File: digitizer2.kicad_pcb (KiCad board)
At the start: 2 copper layers, 3 parts, among them U1 XC7A35T, U3 MT41K128M16, U4 ADS5403

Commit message: Initial routing
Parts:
- moved U4 24.7 mm to (160.0, 120.0), turned to 270 degrees
- moved U1 22.5 mm to (160.0, 95.0), turned to 135 degrees
- moved U3 18.7 mm to (140.0, 95.0), turned to 180 degrees
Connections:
- net Net-(U1-PadL7) renamed /JTAG_TCK
- net Net-(U1-PadM7) renamed /JTAG_TMS
- net Net-(U1-PadN7) renamed /JTAG_TDI
- net Net-(U1-PadN8) renamed /JTAG_TDO
- net Net-(U3-PadA2) renamed /DRAM_DQ13
- net Net-(U3-PadA3) renamed /DRAM_DQ15
- net Net-(U3-PadA7) renamed /DRAM_DQ12
- net Net-(U3-PadB7) renamed /DRAM_DQS1_N
- net Net-(U3-PadB8) renamed /DRAM_DQ14
- net Net-(U3-PadC2) renamed /DRAM_DQ11
- net Net-(U3-PadC3) renamed /DRAM_DQ9
- net Net-(U3-PadC7) renamed /DRAM_DQS1_P
- net Net-(U3-PadC8) renamed /DRAM_DQ10
- net Net-(U3-PadD3) renamed /DRAM_DM1
- net Net-(U3-PadD7) renamed /DRAM_DQ8
- net Net-(U3-PadE3) renamed /DRAM_DQ0
- net Net-(U3-PadE7) renamed /DRAM_DM0
- net Net-(U3-PadF2) renamed /DRAM_DQ2
- net Net-(U3-PadF3) renamed /DRAM_DQS0_P
- net Net-(U3-PadF7) renamed /DRAM_DQ1
- net Net-(U3-PadF8) renamed /DRAM_DQ3
- net Net-(U3-PadG2) renamed /DRAM_DQ6
- net Net-(U3-PadG3) renamed /DRAM_DQS0_N
- net Net-(U3-PadH3) renamed /DRAM_DQ4
- net Net-(U3-PadH7) renamed /DRAM_DQ7
- net Net-(U3-PadH8) renamed /DRAM_DQ5
- net Net-(U3-PadJ3) renamed /DRAM_RAS
- net Net-(U3-PadJ7) renamed /DRAM_CK_P
- net Net-(U3-PadK1) renamed /DRAM_ODT
- net Net-(U3-PadK3) renamed /DRAM_CAS
- net Net-(U3-PadK7) renamed /DRAM_CK_N
- net Net-(U3-PadK9) renamed /DRAM_CKE
- net Net-(U3-PadL2) renamed /DRAM_CS
- net Net-(U3-PadL3) renamed /DRAM_WE
- net Net-(U3-PadL7) renamed /DRAM_A10
- net Net-(U3-PadL8) renamed /DRAM_ZQ
- net Net-(U3-PadM2) renamed /DRAM_BA0
- net Net-(U3-PadM3) renamed /DRAM_BA2
- net Net-(U3-PadN2) renamed /DRAM_A3
- net Net-(U3-PadN3) renamed /DRAM_A0
- net Net-(U3-PadN7) renamed /DRAM_A12
- net Net-(U3-PadN8) renamed /DRAM_BA1
- net Net-(U3-PadP2) renamed /DRAM_A5
- net Net-(U3-PadP3) renamed /DRAM_A2
- net Net-(U3-PadP7) renamed /DRAM_A1
- net Net-(U3-PadP8) renamed /DRAM_A4
- net Net-(U3-PadR2) renamed /DRAM_A7
- net Net-(U3-PadR3) renamed /DRAM_A9
- net Net-(U3-PadR7) renamed /DRAM_A11
- net Net-(U3-PadR8) renamed /DRAM_A6
- net Net-(U3-PadT2) renamed /DRAM_RESET
- net Net-(U3-PadT3) renamed /DRAM_A13
- net Net-(U3-PadT8) renamed /DRAM_A8
- net Net-(U4-PadA10) renamed /ADC_SDO
- net Net-(U4-PadA11) renamed /ADC_SDIO
- net Net-(U4-PadA12) renamed /ADC_SCLK
- net Net-(U4-PadA13) renamed /ADC_SDENB
- net Net-(U4-PadH1) renamed /ADC_DACLK_N
- net Net-(U4-PadH2) renamed /ADC_DACLK_P
- net Net-(U4-PadH3) renamed /ADC_DA0_N
- net Net-(U4-PadH4) renamed /ADC_DA0_P
- net Net-(U4-PadJ1) renamed /ADC_DA1_N
- net Net-(U4-PadJ2) renamed /ADC_DA1_P
- net Net-(U4-PadJ3) renamed /ADC_DA2_N
- net Net-(U4-PadJ4) renamed /ADC_DA2_P
- net Net-(U4-PadK1) renamed /ADC_DA3_N
- net Net-(U4-PadK2) renamed /ADC_DA3_P
- net Net-(U4-PadK3) renamed /ADC_DA4_N
- net Net-(U4-PadK4) renamed /ADC_DA4_P
- net Net-(U4-PadL1) renamed /ADC_DA5_N
- net Net-(U4-PadL2) renamed /ADC_DA5_P
- net Net-(U4-PadL3) renamed /ADC_DA6_N
- net Net-(U4-PadL4) renamed /ADC_DA6_P
- net Net-(U4-PadL5) renamed /ADC_OVRA_N
- net Net-(U4-PadM1) renamed /ADC_DA7_N
- net Net-(U4-PadM2) renamed /ADC_DA7_P
- net Net-(U4-PadM3) renamed /ADC_DA8_N
- net Net-(U4-PadM4) renamed /ADC_DA8_P
- net Net-(U4-PadM5) renamed /ADC_OVRA_P
- net Net-(U4-PadN1) renamed /ADC_DA9_N
- net Net-(U4-PadN2) renamed /ADC_DA10_N
- net Net-(U4-PadN3) renamed /ADC_DA11_N
- net Net-(U4-PadP1) renamed /ADC_DA9_P
- net Net-(U4-PadP2) renamed /ADC_DA10_P
- net Net-(U4-PadP3) renamed /ADC_DA11_P
- U3 pad A8: Net-(U3-PadA8) -> Net-(U3-PadA1)
- U3 pad B3: Net-(U3-PadB3) -> Net-(U3-PadA9)
- U3 pad B9: Net-(U3-PadB9) -> Net-(U3-PadB1)
- U3 pad C1: Net-(U3-PadC1) -> Net-(U3-PadA1)
- U3 pad C9: Net-(U3-PadC9) -> Net-(U3-PadA1)
- U3 pad D1: Net-(U3-PadD1) -> Net-(U3-PadB1)
- U3 pad D2: Net-(U3-PadD2) -> Net-(U3-PadA1)
- U3 pad D8: Net-(U3-PadD8) -> Net-(U3-PadB1)
- U3 pad D9: Net-(U3-PadD9) -> Net-(U3-PadB2)
- U3 pad E1: Net-(U3-PadE1) -> Net-(U3-PadA9)
- U3 pad E2: Net-(U3-PadE2) -> Net-(U3-PadB1)
- U3 pad E8: Net-(U3-PadE8) -> Net-(U3-PadB1)
- U3 pad E9: Net-(U3-PadE9) -> Net-(U3-PadA1)
- U3 pad F1: Net-(U3-PadF1) -> Net-(U3-PadA1)
- U3 pad F9: Net-(U3-PadF9) -> Net-(U3-PadB1)
- U3 pad G1: Net-(U3-PadG1) -> Net-(U3-PadB1)
- U3 pad G7: Net-(U3-PadG7) -> Net-(U3-PadB2)
- U3 pad G8: Net-(U3-PadG8) -> Net-(U3-PadA9)
- U3 pad G9: Net-(U3-PadG9) -> Net-(U3-PadB1)
- U3 pad H2: Net-(U3-PadH2) -> Net-(U3-PadA1)
- U3 pad H9: Net-(U3-PadH9) -> Net-(U3-PadA1)
- U3 pad J2: Net-(U3-PadJ2) -> Net-(U3-PadA9)
- U3 pad J8: Net-(U3-PadJ8) -> Net-(U3-PadA9)
- U3 pad K2: Net-(U3-PadK2) -> Net-(U3-PadB2)
- U3 pad K8: Net-(U3-PadK8) -> Net-(U3-PadB2)
- U3 pad M1: Net-(U3-PadM1) -> Net-(U3-PadA9)
- U3 pad M9: Net-(U3-PadM9) -> Net-(U3-PadA9)
- U3 pad N1: Net-(U3-PadN1) -> Net-(U3-PadB2)
- U3 pad N9: Net-(U3-PadN9) -> Net-(U3-PadB2)
- U3 pad P1: Net-(U3-PadP1) -> Net-(U3-PadA9)
- U3 pad P9: Net-(U3-PadP9) -> Net-(U3-PadA9)
- U3 pad R1: Net-(U3-PadR1) -> Net-(U3-PadB2)
- U3 pad R9: Net-(U3-PadR9) -> Net-(U3-PadB2)
- U3 pad T1: Net-(U3-PadT1) -> Net-(U3-PadA9)
- U3 pad T9: Net-(U3-PadT9) -> Net-(U3-PadA9)
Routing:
- net /DRAM_DQ8: track 0.00 -> 20.3 mm, vias 0 -> 1
- net /DRAM_DQ10: track 0.00 -> 18.8 mm, vias 0 -> 1
- net /DRAM_DQ12: track 0.00 -> 17.6 mm, vias 0 -> 1
- net /DRAM_DQS1_N: track 0.00 -> 17.3 mm, vias 0 -> 1
- net /DRAM_DQ14: track 0.00 -> 17.2 mm, vias 0 -> 1
- net /DRAM_DQS1_P: track 0.00 -> 16.8 mm, vias 0 -> 1
- net /DRAM_DQ13: track 0.00 -> 15.7 mm, vias 0 -> 1
- net /DRAM_DQ15: track 0.00 -> 15.7 mm, vias 0 -> 1
- net /ADC_DA4_P: track 0.00 -> 14.9 mm, vias 0 -> 1
- net /ADC_DA4_N: track 0.00 -> 14.3 mm, vias 0 -> 1
- net /ADC_OVRA_P: track 0.00 -> 13.9 mm, vias 0 -> 1
- net /ADC_DA2_P: track 0.00 -> 13.7 mm, vias 0 -> 1
- net /ADC_DA0_P: track 0.00 -> 13.6 mm, vias 0 -> 1
- net /ADC_OVRA_N: track 0.00 -> 13.6 mm, vias 0 -> 1
- net /ADC_DA11_N: track 0.00 -> 13.1 mm, vias 0 -> 1
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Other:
- copper layers 2 -> 6
- net class Default: clearance 0.2 -> 0.125; trace_width 0.25 -> 0.13; via_dia 0.6 -> 0.5; via_drill 0.4 -> 0.15
- rule pad_to_mask_clearance: 0.2 -> 0.05
- rule trace_clearance: 0.2 -> 0.125
- rule trace_min: 0.2 -> 0.125
- rule via_min_drill: 0.3 -> 0.15
- rule via_min_size: 0.4 -> 0.5

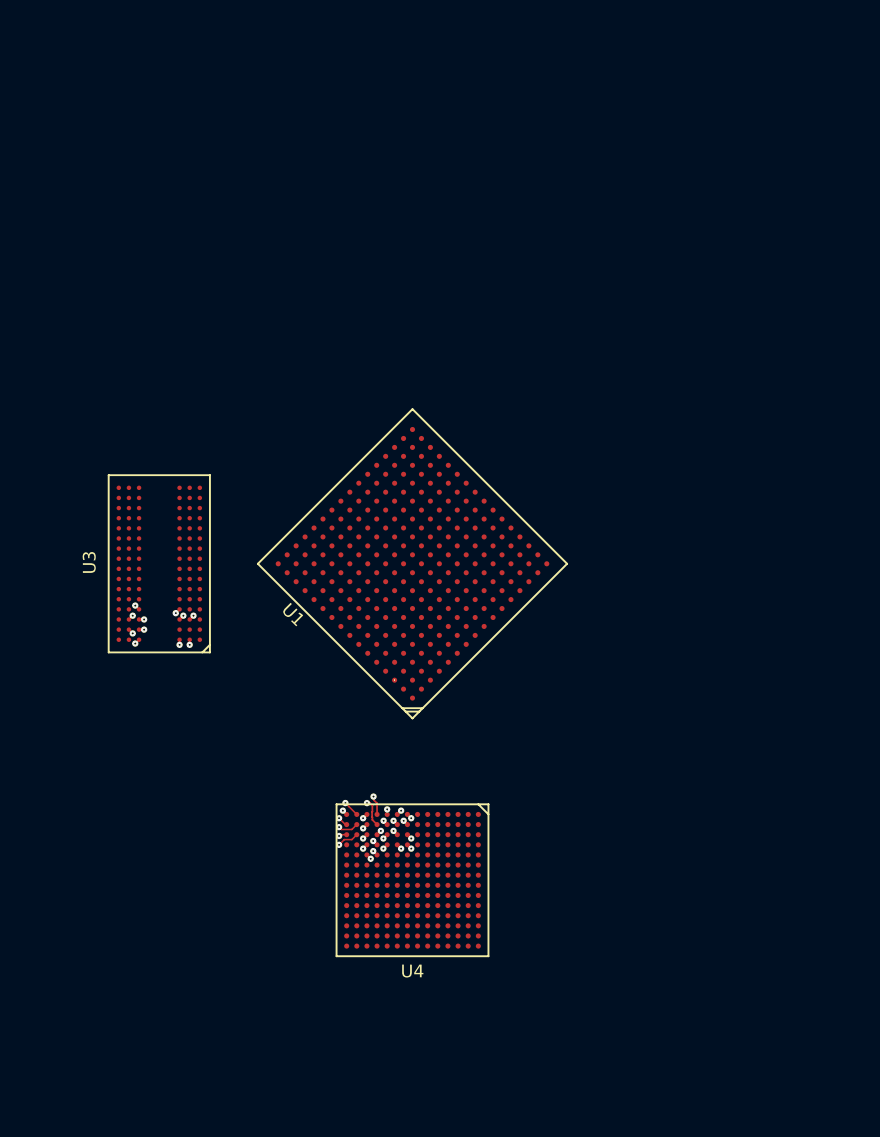
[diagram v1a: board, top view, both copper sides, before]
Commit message: Tuned ADC DDR layout
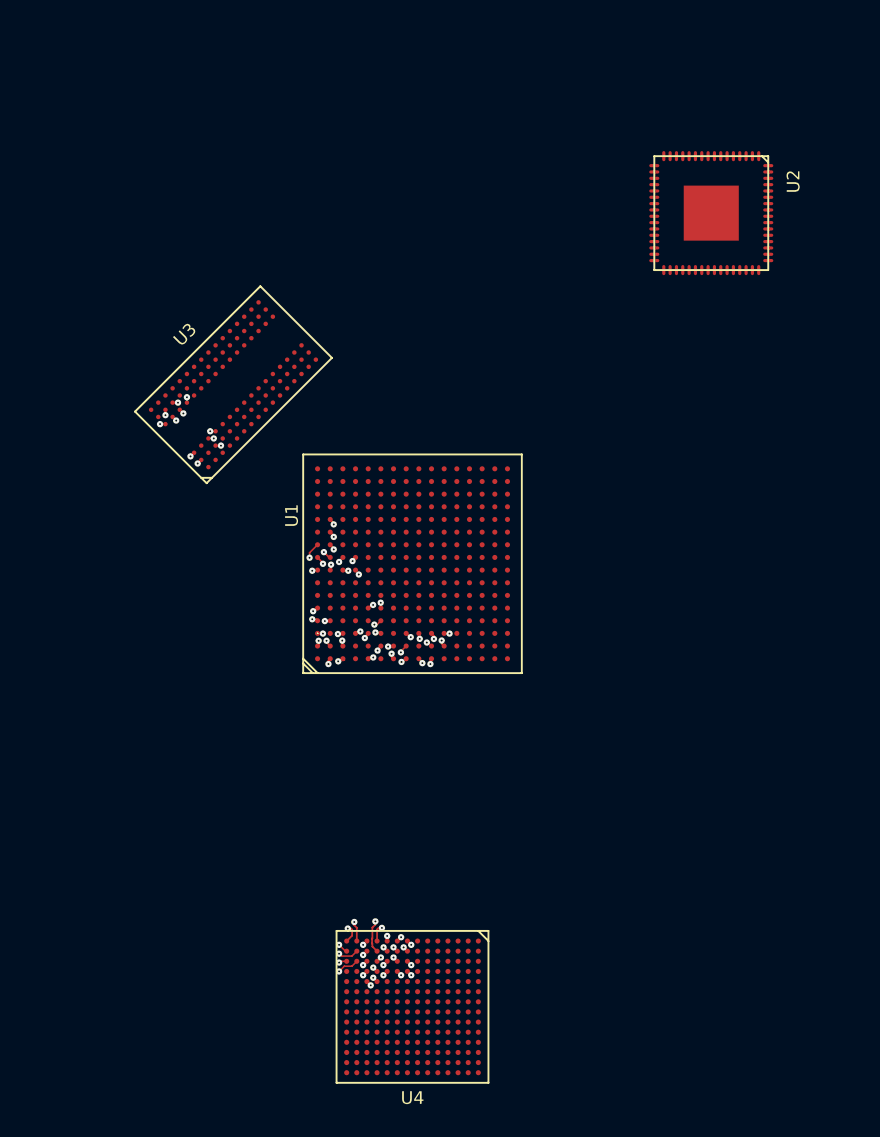
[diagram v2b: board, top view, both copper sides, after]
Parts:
- added U2: FT2232H, digitizer2_modules:QFN-FT2232HQ-64_pitch0.5, F.Cu at (183.6, 67.3)
- moved U3 15.3 mm to (145.9, 80.9), turned to 135 degrees
- moved U4 10.0 mm to (160.0, 130.0)
- turned U1 to 90 degrees
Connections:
- net Net-(U1-PadA4) renamed /ADC_SAMPLE_CLK_N
- net Net-(U1-PadA5) renamed /ADC_SAMPLE_CLK_P
- net Net-(U4-PadA14) renamed /ADC_VREF
- net Net-(U4-PadB14) renamed /ADC_VCM
- net Net-(U4-PadK14) renamed /ADC_INA_P
- net Net-(U4-PadL14) renamed /ADC_INA_N
- net Net-(U4-PadP13) renamed /ADC_CLKIN_N
- net Net-(U4-PadP14) renamed /ADC_CLKIN_P
- U1 pad A10: Net-(U1-PadA10) -> /DRAM_DQS1_N
- U1 pad A2: Net-(U1-PadA2) -> /ADC_DA10_N
- U1 pad A3: Net-(U1-PadA3) -> /ADC_OVRA_N
- U1 pad A8: Net-(U1-PadA8) -> /DRAM_DQ15
- U1 pad A9: Net-(U1-PadA9) -> /DRAM_DQ10
- U1 pad B1: Net-(U1-PadB1) -> /ADC_DA8_P
- U1 pad B10: Net-(U1-PadB10) -> /DRAM_DM1
- U1 pad B11: Net-(U1-PadB11) -> /DRAM_DQ11
- U1 pad B12: Net-(U1-PadB12) -> /DRAM_DQ9
- U1 pad B2: Net-(U1-PadB2) -> /ADC_DA10_P
- U1 pad B4: Net-(U1-PadB4) -> /ADC_OVRA_P
- U1 pad B9: Net-(U1-PadB9) -> /DRAM_DQS1_P
- U1 pad C1: Net-(U1-PadC1) -> /ADC_DA8_N
- U1 pad C2: Net-(U1-PadC2) -> /ADC_DA11_P
- U1 pad C3: Net-(U1-PadC3) -> /ADC_DA11_N
- U1 pad C8: Net-(U1-PadC8) -> /DRAM_DQ14
- U1 pad C9: Net-(U1-PadC9) -> /DRAM_DQ8
- U1 pad D3: Net-(U1-PadD3) -> /ADC_DA9_P
- U1 pad D8: Net-(U1-PadD8) -> /DRAM_DQ12
- U1 pad D9: Net-(U1-PadD9) -> /DRAM_DQ13
- U1 pad E1: Net-(U1-PadE1) -> /ADC_DA7_P
- U1 pad E3: Net-(U1-PadE3) -> /ADC_DA9_N
- U1 pad E5: Net-(U1-PadE5) -> /ADC_DACLK_P
- U1 pad F2: Net-(U1-PadF2) -> /ADC_DA7_N
- U1 pad F3: Net-(U1-PadF3) -> /ADC_DA6_N
- U1 pad F4: Net-(U1-PadF4) -> /ADC_DA6_P
- U1 pad F5: Net-(U1-PadF5) -> /ADC_DACLK_N
- U1 pad G1: Net-(U1-PadG1) -> /ADC_DA5_N
- U1 pad G2: Net-(U1-PadG2) -> /ADC_DA5_P
- U1 pad H1: Net-(U1-PadH1) -> /ADC_DA1_N
- U1 pad H2: Net-(U1-PadH2) -> /ADC_DA1_P
- U1 pad H3: Net-(U1-PadH3) -> /ADC_DA3_N
- U1 pad J1: Net-(U1-PadJ1) -> /ADC_DA2_N
- U1 pad J3: Net-(U1-PadJ3) -> /ADC_DA3_P
- U1 pad K1: Net-(U1-PadK1) -> /ADC_DA2_P
- U1 pad K2: Net-(U1-PadK2) -> /ADC_DA0_N
- U1 pad K3: Net-(U1-PadK3) -> /ADC_DA0_P
- U1 pad L2: Net-(U1-PadL2) -> /ADC_DA4_N
- U1 pad L3: Net-(U1-PadL3) -> /ADC_DA4_P
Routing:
- net /ADC_DA5_P: track 10.1 -> 38.0 mm, vias 1 -> 2
- net /ADC_DA9_P: track 8.62 -> 35.2 mm, vias 1 -> 2
- net /ADC_DA9_N: track 8.96 -> 35.3 mm, vias 1 -> 2
- net /ADC_DA1_N: track 8.79 -> 34.9 mm, vias 1 -> 2
- net /ADC_DA5_N: track 9.22 -> 35.2 mm, vias 1 -> 2
- net /ADC_DA10_P: track 9.62 -> 35.4 mm, vias 1 -> 2
- net /ADC_DA3_N: track 9.43 -> 34.8 mm, vias 1 -> 2
- net /ADC_DA1_P: track 9.68 -> 34.9 mm, vias 1 -> 2
- net /ADC_DACLK_N: track 10.0 -> 34.9 mm, vias 1 -> 2
- net /ADC_DA6_N: track 10.8 -> 35.3 mm, vias 1 -> 2
- net /ADC_DA7_N: track 10.9 -> 35.3 mm, vias 1 -> 2
- net /ADC_DACLK_P: track 10.4 -> 34.8 mm, vias 1 -> 2
- net /ADC_DA3_P: track 10.6 -> 34.8 mm, vias 1 -> 2
- net /ADC_DA10_N: track 11.3 -> 35.4 mm, vias 1 -> 2
- net /ADC_DA6_P: track 11.4 -> 35.3 mm, vias 1 -> 2
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
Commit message: Changed LVDS layout. Try new DRAM position.
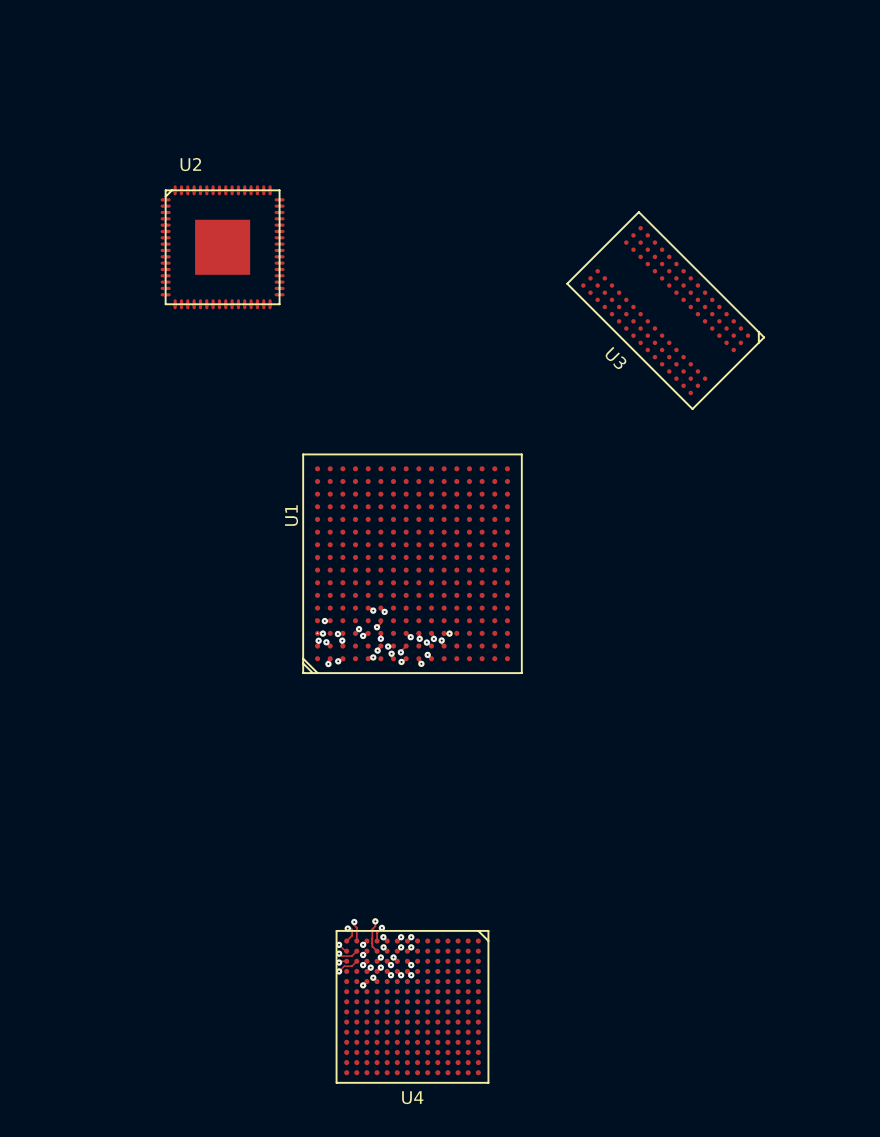
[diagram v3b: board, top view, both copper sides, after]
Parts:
- moved U2 38.7 mm to (145.0, 70.0), turned to 0 degrees
- moved U3 34.6 mm to (180.0, 75.0), turned to 225 degrees
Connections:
- U1 pad A10: /DRAM_DQS1_N -> Net-(U1-PadA10)
- U1 pad A2: /ADC_DA10_N -> /ADC_OVRA_P
- U1 pad A3: /ADC_OVRA_N -> /ADC_DA10_P
- U1 pad A8: /DRAM_DQ15 -> Net-(U1-PadA8)
- U1 pad A9: /DRAM_DQ10 -> Net-(U1-PadA9)
- U1 pad B10: /DRAM_DM1 -> Net-(U1-PadB10)
- U1 pad B11: /DRAM_DQ11 -> Net-(U1-PadB11)
- U1 pad B12: /DRAM_DQ9 -> Net-(U1-PadB12)
- U1 pad B2: /ADC_DA10_P -> /ADC_OVRA_N
- U1 pad B4: /ADC_OVRA_P -> /ADC_DA10_N
- U1 pad B9: /DRAM_DQS1_P -> Net-(U1-PadB9)
- U1 pad C8: /DRAM_DQ14 -> Net-(U1-PadC8)
- U1 pad C9: /DRAM_DQ8 -> Net-(U1-PadC9)
- U1 pad D8: /DRAM_DQ12 -> Net-(U1-PadD8)
- U1 pad D9: /DRAM_DQ13 -> Net-(U1-PadD9)
- U1 pad E5: /ADC_DACLK_P -> /ADC_DACLK_N
- U1 pad F5: /ADC_DACLK_N -> /ADC_DACLK_P
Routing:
- net /DRAM_DQ12: track 23.6 -> 0.00 mm, vias 2 -> 0
- net /DRAM_DQ14: track 22.8 -> 0.00 mm, vias 2 -> 0
- net /DRAM_DQ8: track 19.7 -> 0.00 mm, vias 2 -> 0
- net /DRAM_DQ10: track 19.5 -> 0.00 mm, vias 2 -> 0
- net /DRAM_DQ13: track 17.8 -> 0.00 mm, vias 2 -> 0
- net /DRAM_DQS1_P: track 17.7 -> 0.00 mm, vias 2 -> 0
- net /DRAM_DQS1_N: track 17.5 -> 0.00 mm, vias 2 -> 0
- net /DRAM_DQ9: track 16.0 -> 0.00 mm, vias 2 -> 0
- net /DRAM_DM1: track 15.3 -> 0.00 mm, vias 2 -> 0
- net /DRAM_DQ15: track 14.7 -> 0.00 mm, vias 2 -> 0
- net /DRAM_DQ11: track 13.4 -> 0.00 mm, vias 2 -> 0
- net /ADC_SAMPLE_CLK_P: track 5.33 -> 0.00 mm, vias 1 -> 0
- net /ADC_SAMPLE_CLK_N: track 5.10 -> 0.17 mm, vias 1 -> 0
- net /ADC_DA5_P: track 38.0 -> 34.9 mm
- net /ADC_OVRA_P: track 37.3 -> 35.0 mm
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
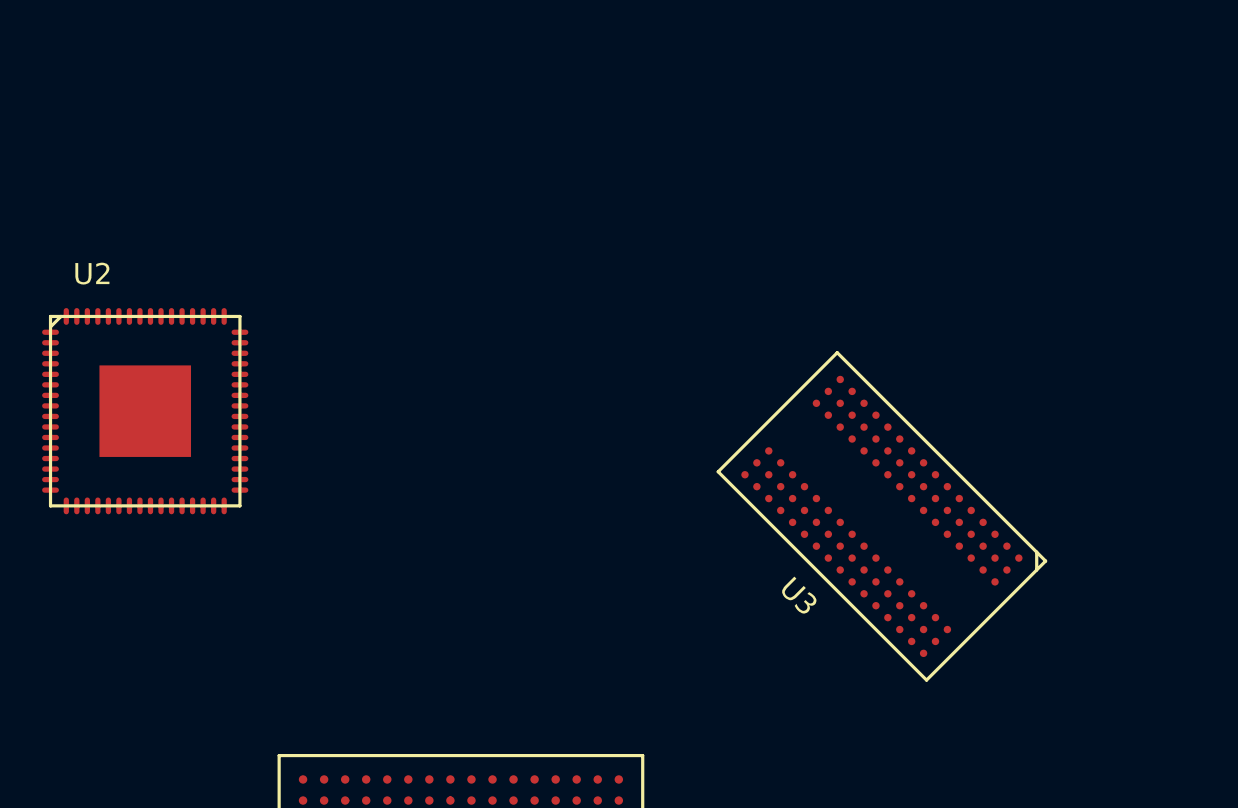
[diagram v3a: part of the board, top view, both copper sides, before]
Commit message: Choose final DDR3 part (MT41K and MT41J pin compatible)
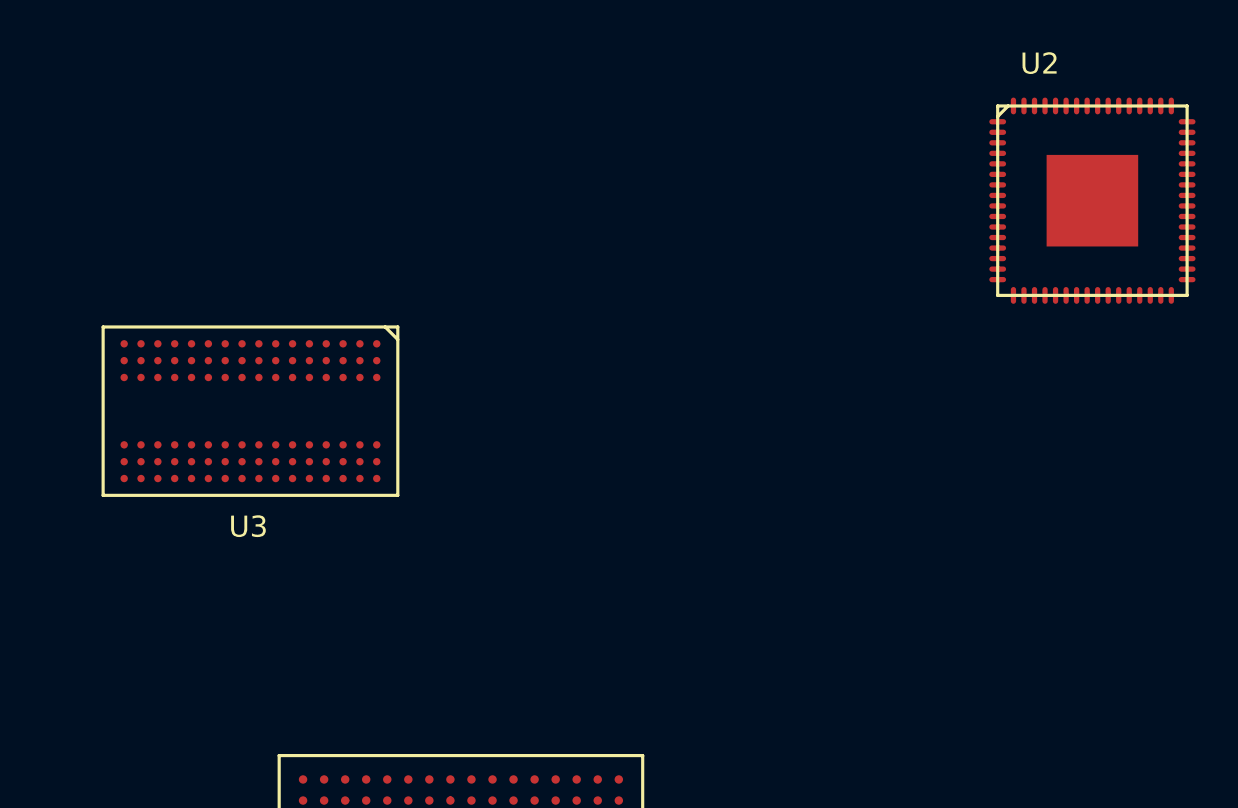
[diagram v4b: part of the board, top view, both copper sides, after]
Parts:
- U3: value MT41K128M16 -> MT41J128M16
- moved U2 46.1 mm to (190.0, 60.0)
- moved U3 30.4 mm to (150.0, 70.0), turned to 270 degrees
